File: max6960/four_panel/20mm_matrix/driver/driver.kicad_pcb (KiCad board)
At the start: 4 copper layers, 40 x 40 mm, 10 parts, among them P1 LED-MATRIX-2X-8X8, P2 LED-MATRIX-2X-8X8, P3 CONN15, P4 CONN15, U1 MAX6960, U2 74AHC1G126, U3 MAX6960

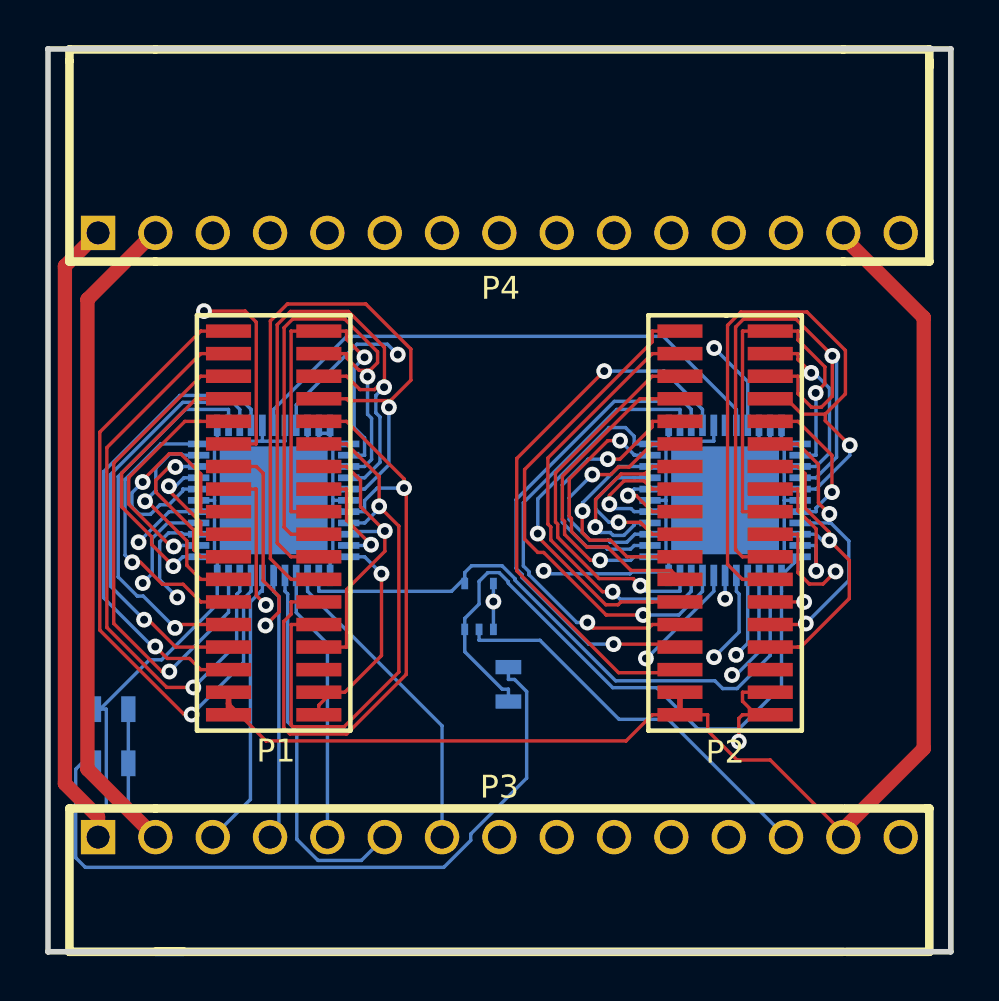
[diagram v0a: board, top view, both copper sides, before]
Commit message: Re-routed four matrix panel driver and adapter. Switched to board-to-board connectors from major league.
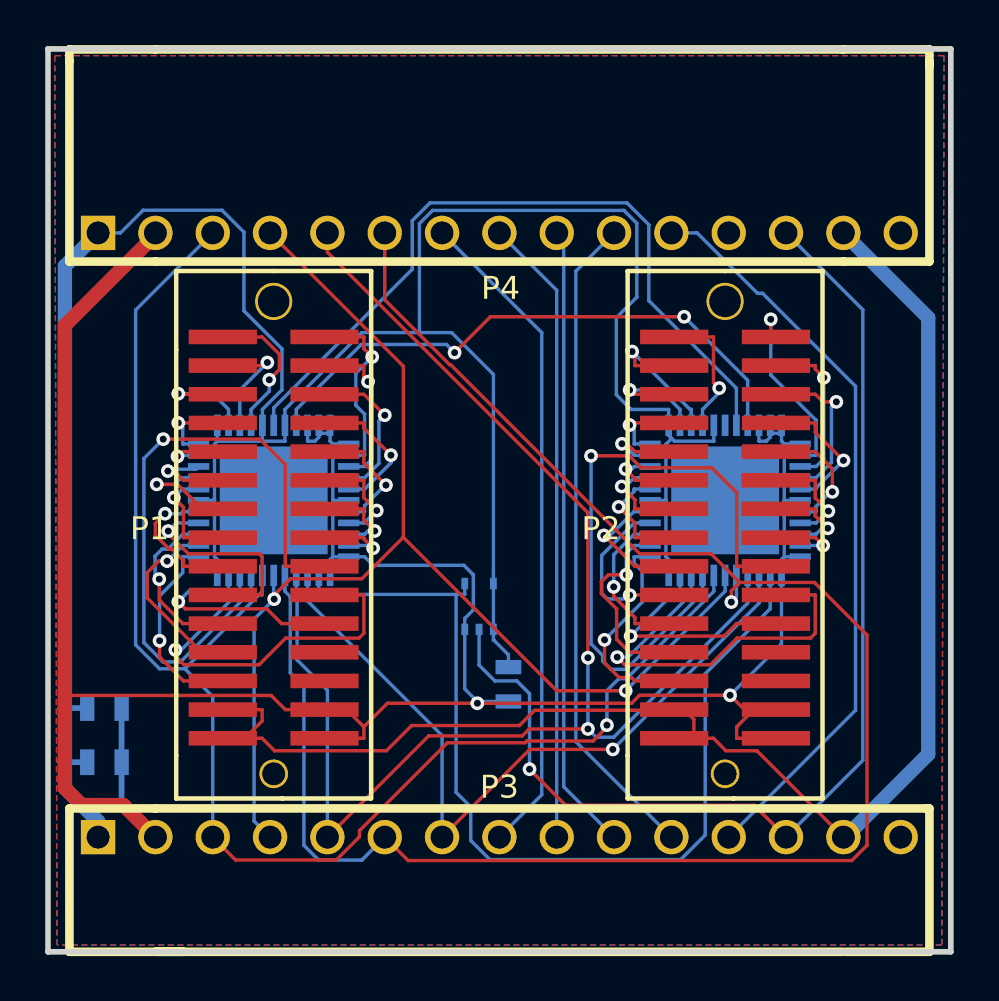
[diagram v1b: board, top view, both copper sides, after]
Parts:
- P1, P2: value LED-MATRIX-2X-8X8 -> CONN15X2; footprint SMD_HEADER_18X2 -> SMD_PIN_ARRAY_M_0P5IN_15X2
- moved P1 0.65 mm to (60.0, 71.7)
- moved P2 0.65 mm to (80.0, 71.7)
- moved C1 0.30 mm to (52.5, 81.6)
- moved C3 0.30 mm to (52.5, 79.2)
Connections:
- C1 pad 1: N-0000048 -> /V+
- C2 pad 1: N-0000048 -> /V+
- P1 pad 1: /COL_A1 -> /COL_A16
- P1 pad 11: /COL_A6 -> /COL_A11
- P1 pad 13: /COL_A7 -> /COL_A10
- P1 pad 15: /COL_A8 -> /COL_A9
- P1 pad 17: /COL_A9 -> /COL_A8
- P1 pad 18: /ROW_A1 -> /COL_A1
- P1 pad 19: /COL_A10 -> /COL_A7
- P1 pad 20: /ROW_A2 -> /COL_A2
- P1 pad 21: /COL_A11 -> /COL_A6
- P1 pad 22: /ROW_A3 -> /COL_A3
- P1 pad 23: /COL_A12 -> /COL_A5
- P1 pad 24: /ROW_A4 -> N-0000051
- P1 pad 25: /COL_A13 -> /COL_A4
- P1 pad 26: /ROW_A5 -> N-0000053
- P1 pad 27: /COL_A14 -> /VAUX
- P1 pad 28: /ROW_A6 -> GND
- P1 pad 29: /COL_A15 -> /VAUX
- P1 pad 3: /COL_A2 -> /COL_A15
- P1 pad 30: /ROW_A7 -> GND
- P1 pad 5: /COL_A3 -> /COL_A14
- P1 pad 7: /COL_A4 -> /COL_A13
- P1 pad 9: /COL_A5 -> /COL_A12
- P2 pad 1: /COL_B1 -> /COL_B16
- P2 pad 11: /COL_B6 -> /COL_B11
- P2 pad 13: /COL_B7 -> /COL_B10
- P2 pad 15: /COL_B8 -> /COL_B9
- P2 pad 17: /COL_B9 -> /COL_B8
- P2 pad 18: /ROW_B1 -> /COL_B1
- P2 pad 19: /COL_B10 -> /COL_B7
- P2 pad 20: /ROW_B2 -> /COL_B2
- P2 pad 21: /COL_B11 -> /COL_B6
- P2 pad 22: /ROW_B3 -> /COL_B3
- P2 pad 23: /COL_B12 -> /COL_B5
- P2 pad 24: /ROW_B4 -> N-0000061
- P2 pad 25: /COL_B13 -> /COL_B4
- P2 pad 26: /ROW_B5 -> N-0000058
- P2 pad 27: /COL_B14 -> /VAUX
- P2 pad 28: /ROW_B6 -> GND
- P2 pad 29: /COL_B15 -> /VAUX
- P2 pad 3: /COL_B2 -> /COL_B15
- P2 pad 30: /ROW_B7 -> GND
- P2 pad 5: /COL_B3 -> /COL_B14
- P2 pad 7: /COL_B4 -> /COL_B13
- P2 pad 9: /COL_B5 -> /COL_B12
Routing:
- net N-0000048: track 32.2 -> 0.00 mm
- net GND: track 146.6 -> 117.8 mm
- net /ROW_A4: track 31.4 -> 6.35 mm
- net /ROW_A5: track 30.3 -> 5.92 mm
- net /V+: track 97.1 -> 120.8 mm, vias 2 -> 0
- net /ROW_B4: track 29.9 -> 6.40 mm
- net /ROW_B3: track 29.0 -> 7.25 mm
- net /ROW_A3: track 27.6 -> 6.90 mm
- net /ROW_A6: track 25.5 -> 4.79 mm
- net /COL_A6: track 27.0 -> 7.60 mm, vias 2 -> 1
- net /COL_B16: track 25.4 -> 6.07 mm
- net /ROW_A2: track 24.2 -> 7.19 mm
- net /COL_B15: track 22.2 -> 6.80 mm
- net /ROW_B2: track 22.5 -> 7.21 mm, vias 2 -> 1
- net /COL_B14: track 20.4 -> 5.35 mm
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- added copper zone on B.Cu, net /V+
- added copper zone on F.Cu, net GND
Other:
- copper layers 4 -> 2
- net class Default: via_dia 0.7 -> 0.6096; via_drill 0.35 -> 0.3048
- rule via_min_drill: 0.35 -> 0.3048
- rule via_min_size: 0.7 -> 0.6096

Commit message: Created gerber files and BOM for 4-matrix atmega328 and max6960 PCBs.
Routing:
- removed copper zone on B.Cu, net /V+
- removed copper zone on F.Cu, net GND
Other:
- board text added: "4-Matrix MAX6960 Driver v0.1 www.iorodeo.com"
- board text removed: "4-Matrix MAX6960 Driver IO Rodeo Inc. v1.0"
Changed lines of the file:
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@@
     (visible_elements FFFFFF7F)
     (pcbplotparams
-      (layerselection 3178497)
+      (layerselection 284196865)
       (usegerberextensions true)
       (excludeedgelayer true)
@@
       (outputformat 1)
       (mirror false)
-      (drillshape 1)
+      (drillshape 0)
       (scaleselection 1)
-      (outputdirectory ""))
+      (outputdirectory gerber_v0p1/))
   )
   (net 0 "")
@@
     )
   )
-  (gr_text "4-Matrix MAX6960 Driver\nIO Rodeo Inc. v1.0" (at 69.5 52) (layer B.SilkS)
+  (gr_text "4-Matrix MAX6960 Driver v0.1\nwww.iorodeo.com" (at 69.5 52) (layer B.SilkS)
     (effects (font (size 1.016 1.016) (thickness 0.2032)) (justify mirror))
   )
@@
   (segment (start 75.8571 78.9891) (end 76.2113 78.6349) (width 0.1524) (layer F.Cu) (net 65))
   (segment (start 69.024 78.9891) (end 75.8571 78.9891) (width 0.1524) (layer F.Cu) (net 65))
-  (zone (net 63) (net_name /V+) (layer B.Cu) (hatch edge 0.508)
-    (connect_pads (clearance 0.127))
-    (min_thickness 0.127)
-    (fill (arc_segments 16) (thermal_gap 0.635) (thermal_bridge_width 0.254))
-    (polygon
-      (pts
-        (xy 89.7 50.3) (xy 89.6 89.7) (xy 50.4 89.7) (xy 50.3 50.3)
-      )
-    )
-  )
-  (zone (net 65) (net_name GND) (layer F.Cu) (hatch edge 0.508)
-    (connect_pads (clearance 0.127))
-    (min_thickness 0.127)
-    (fill (arc_segments 16) (thermal_gap 0.635) (thermal_bridge_width 0.254))
-    (polygon
-      (pts
-        (xy 89.7 50.3) (xy 89.6 89.7) (xy 50.4 89.7) (xy 50.3 50.3)
-      )
-    )
-  )
 )
